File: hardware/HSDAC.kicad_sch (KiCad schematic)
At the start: 75 parts, among them IC1 ES9018K2M, J1 SM07B-SRSS-TB__LF__SN_, J3 USB_C_Receptacle_USB2.0_16P, SW1 RST, U1 CH32V305FBP6, U2 ME6210A33M3G, U3 OPA1678, U4 OPA1678, U5 OPA1678, X1 8M

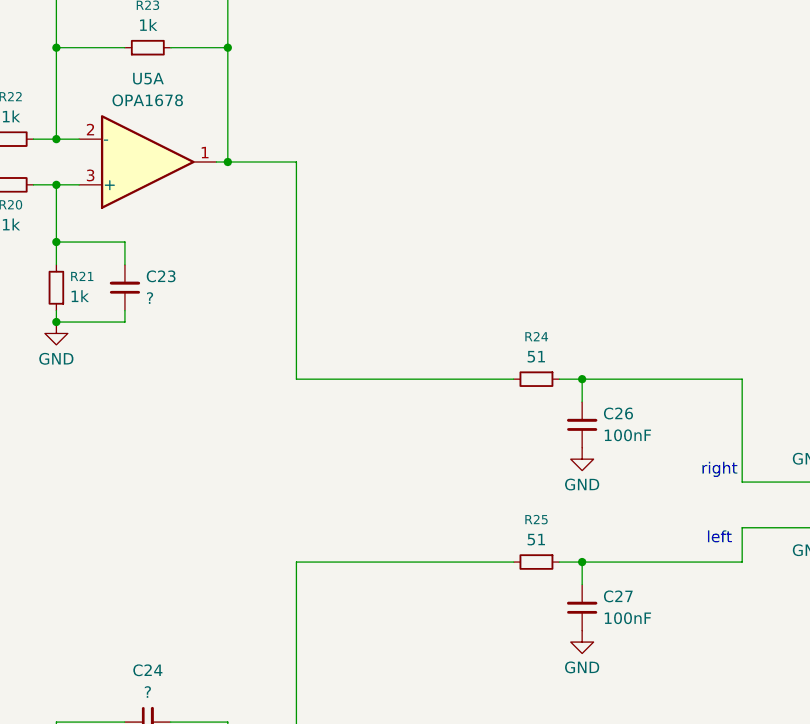
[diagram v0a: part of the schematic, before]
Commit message: 修复声道和运放封装错误
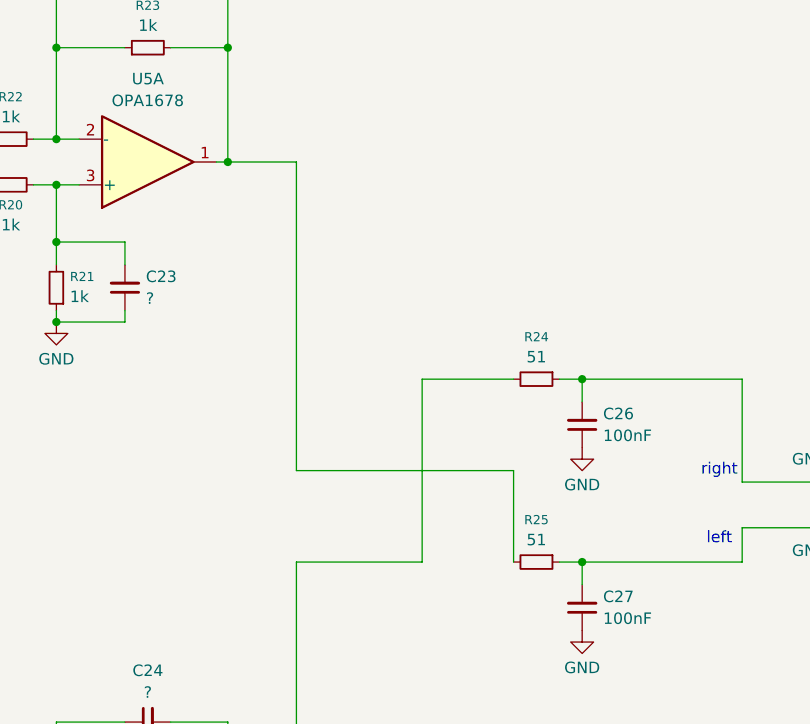
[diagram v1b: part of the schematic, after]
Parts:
- U3, U4, U5: footprint Package_SO:SOIC-8_5.3x6.2mm_P1.27mm -> Package_SO:SOIC-8_3.9x4.9mm_P1.27mm
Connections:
- net at C22.2, R23.2, U5.1: now also R25.2; no longer R24.2
- net at C24.2, R9.2, U5.7: now also R24.2; no longer R25.2
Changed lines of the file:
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@@
 	(wire
 		(pts
+			(xy 292.1 179.07) (xy 292.1 189.23)
+		)
+		(stroke
+			(width 0)
+			(type default)
+		)
+	)
+	(wire
+		(pts
 			(xy 88.9 144.78) (xy 101.6 144.78)
 		)
@@
 	(wire
 		(pts
+			(xy 267.97 144.78) (xy 267.97 179.07)
+		)
+		(stroke
+			(width 0)
+			(type default)
+		)
+	)
+	(wire
+		(pts
 			(xy 124.46 57.15) (xy 124.46 59.69)
 		)
@@
 	(wire
 		(pts
-			(xy 292.1 189.23) (xy 267.97 189.23)
-		)
-		(stroke
-			(width 0)
-			(type default)
-		)
-	)
-	(wire
-		(pts
 			(xy 148.59 49.53) (xy 148.59 59.69)
 		)
@@
 	(wire
 		(pts
-			(xy 267.97 168.91) (xy 267.97 144.78)
-		)
-		(stroke
-			(width 0)
-			(type default)
-		)
-	)
-	(wire
-		(pts
 			(xy 71.12 109.22) (xy 71.12 93.98)
 		)
@@
 	(wire
 		(pts
+			(xy 267.97 189.23) (xy 281.94 189.23)
+		)
+		(stroke
+			(width 0)
+			(type default)
+		)
+	)
+	(wire
+		(pts
 			(xy 20.32 59.69) (xy 27.94 59.69)
 		)
@@
 	(wire
 		(pts
-			(xy 292.1 168.91) (xy 267.97 168.91)
-		)
-		(stroke
-			(width 0)
-			(type default)
-		)
-	)
-	(wire
-		(pts
 			(xy 88.9 139.7) (xy 121.92 139.7)
 		)
@@
 	(wire
 		(pts
+			(xy 281.94 189.23) (xy 281.94 168.91)
+		)
+		(stroke
+			(width 0)
+			(type default)
+		)
+	)
+	(wire
+		(pts
 			(xy 63.5 167.64) (xy 63.5 162.56)
 		)
@@
 	(wire
 		(pts
+			(xy 267.97 179.07) (xy 292.1 179.07)
+		)
+		(stroke
+			(width 0)
+			(type default)
+		)
+	)
+	(wire
+		(pts
 			(xy 88.9 137.16) (xy 142.24 137.16)
 		)
@@
 	(wire
 		(pts
+			(xy 281.94 168.91) (xy 292.1 168.91)
+		)
+		(stroke
+			(width 0)
+			(type default)
+		)
+	)
+	(wire
+		(pts
 			(xy 132.08 59.69) (xy 132.08 49.53)
 		)
@@
 			)
 		)
-		(property "Footprint" "Package_SO:SOIC-8_5.3x6.2mm_P1.27mm"
+		(property "Footprint" "Package_SO:SOIC-8_3.9x4.9mm_P1.27mm"
 			(at 215.9 163.83 0)
 			(effects
@@
 			)
 		)
-		(property "Footprint" "Package_SO:SOIC-8_5.3x6.2mm_P1.27mm"
+		(property "Footprint" "Package_SO:SOIC-8_3.9x4.9mm_P1.27mm"
 			(at 215.9 245.11 0)
 			(effects
@@
 			)
 		)
-		(property "Footprint" "Package_SO:SOIC-8_5.3x6.2mm_P1.27mm"
+		(property "Footprint" "Package_SO:SOIC-8_3.9x4.9mm_P1.27mm"
 			(at 229.87 269.24 0)
 			(effects
@@
 			)
 		)
-		(property "Footprint" "Package_SO:SOIC-8_5.3x6.2mm_P1.27mm"
+		(property "Footprint" "Package_SO:SOIC-8_3.9x4.9mm_P1.27mm"
 			(at 251.46 227.33 0)
 			(effects
@@
 			)
 		)
-		(property "Footprint" "Package_SO:SOIC-8_5.3x6.2mm_P1.27mm"
+		(property "Footprint" "Package_SO:SOIC-8_3.9x4.9mm_P1.27mm"
 			(at 256.54 269.24 0)
 			(effects
@@
 			)
 		)
-		(property "Footprint" "Package_SO:SOIC-8_5.3x6.2mm_P1.27mm"
+		(property "Footprint" "Package_SO:SOIC-8_3.9x4.9mm_P1.27mm"
 			(at 251.46 144.78 0)
 			(effects
@@
 			)
 		)
-		(property "Footprint" "Package_SO:SOIC-8_5.3x6.2mm_P1.27mm"
+		(property "Footprint" "Package_SO:SOIC-8_3.9x4.9mm_P1.27mm"
 			(at 215.9 128.27 0)
 			(effects
@@
 			)
 		)
-		(property "Footprint" "Package_SO:SOIC-8_5.3x6.2mm_P1.27mm"
+		(property "Footprint" "Package_SO:SOIC-8_3.9x4.9mm_P1.27mm"
 			(at 204.47 269.24 0)
 			(effects
@@
 			)
 		)
-		(property "Footprint" "Package_SO:SOIC-8_5.3x6.2mm_P1.27mm"
+		(property "Footprint" "Package_SO:SOIC-8_3.9x4.9mm_P1.27mm"
 			(at 215.9 209.55 0)
 			(effects

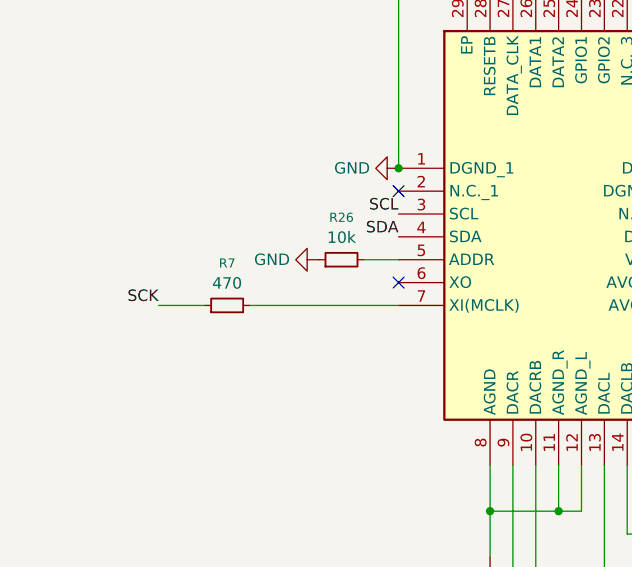
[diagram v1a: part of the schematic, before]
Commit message: SCK的电阻和实际不一样
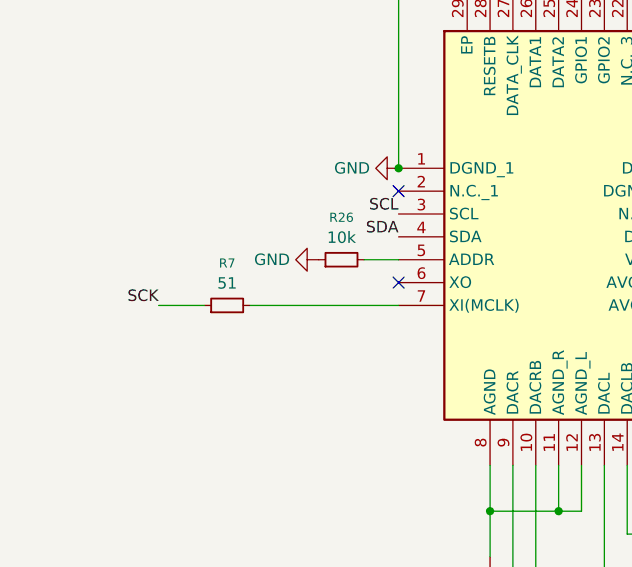
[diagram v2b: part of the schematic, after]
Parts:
- R7: value 470 -> 51
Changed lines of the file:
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@@
 			)
 		)
-		(property "Value" "470"
+		(property "Value" "51"
 			(at 34.29 142.3232 90)
 			(effects
